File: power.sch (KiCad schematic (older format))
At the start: 0 parts

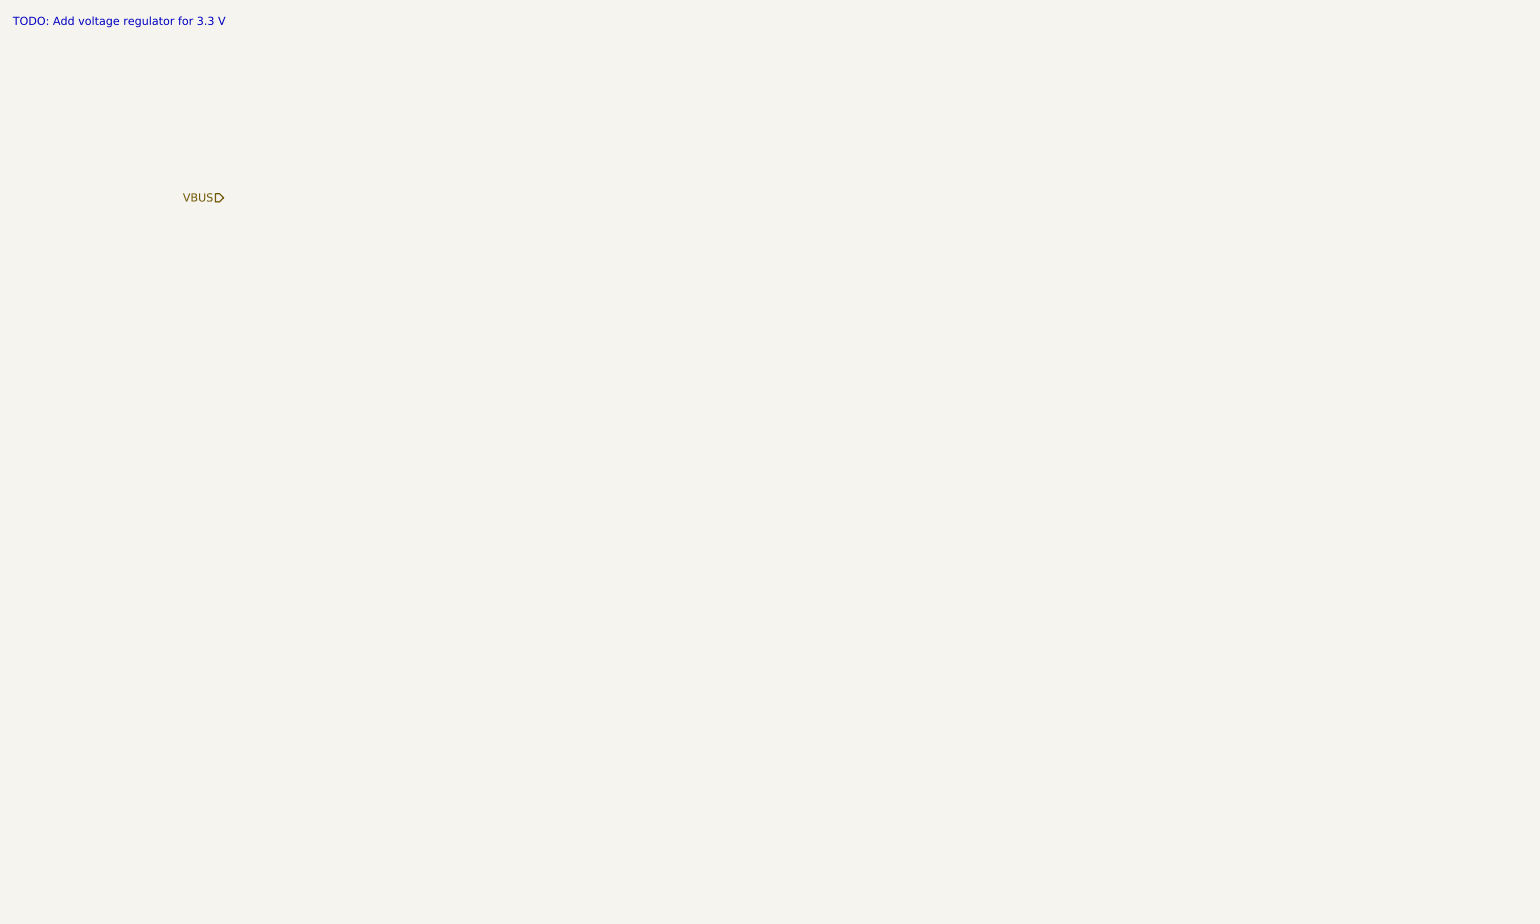
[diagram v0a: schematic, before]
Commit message: Complete muxing and level translation
Added Aux USB to avoid using a HUB, which don't seem to be too readily
available out there and would complicate the design for no good reason.

Now the i2c lines can also be switched.

Added voltage level translation up to 1.2V from 3.3V. Selected
bidirectional level translator.

Started looking into power supply.
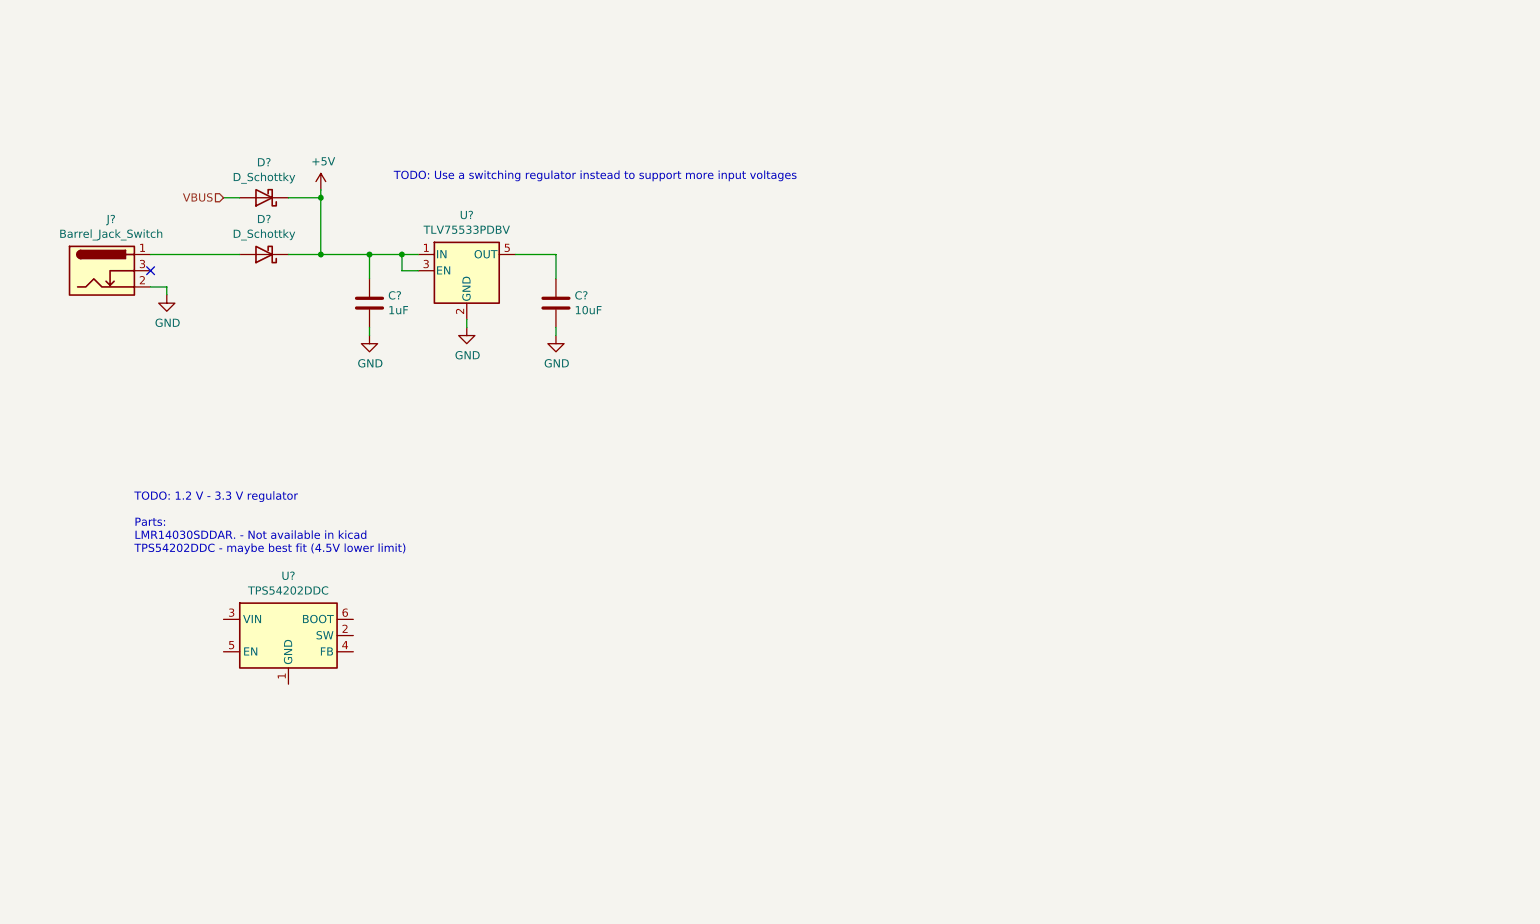
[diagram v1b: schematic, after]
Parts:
- added C?: 1uF, symbol Device:C
- added C?: 10uF, symbol Device:C
- added D? (x2): D_Schottky, symbol Device:D_Schottky
- added J?: Barrel_Jack_Switch, symbol Connector:Barrel_Jack_Switch
- added U?: TLV75533PDBV, Package_TO_SOT_SMD:SOT-23-5, symbol Regulator_Linear:TLV75533PDBV
- added U?: TPS54202DDC, Package_TO_SOT_SMD:SOT-23-6, symbol Regulator_Switching:TPS54202DDC
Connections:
- net VBUS: now also D?.2 (A)
- new net: D?.2 (A), J?.1
- new net: C?.1, U?.5 (OUT)
- new net +5V: C?.1, D?.1 (K), D?.1 (K), U?.1 (IN), U?.3 (EN)
- new net GND: C?.2, C?.2, J?.2, U?.2 (GND)
- no-connect marks 0 -> 1
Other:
- note added: "TODO: 1.2 V - 3.3 V regulator\n\nParts:\nLMR14030SDDAR. - Not available in kicad\nTPS54202DDC - maybe best fit (4.5V lower limit)"
- note added: "TODO: Use a switching regulator instead to support more input voltages"
- note removed: "TODO: Add voltage regulator for 3.3 V"
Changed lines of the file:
@@
 $Descr A4 11693 8268
 encoding utf-8
-Sheet 9 9
+Sheet 11 12
 Title ""
 Date ""
@@
 Text HLabel 2100 1850 0    50   Input ~ 0
 VBUS
-Text Notes 800  800  0    50   ~ 0
-TODO: Add voltage regulator for 3.3 V
+Text Notes 3150 1750 0    50   ~ 0
+TODO: Use a switching regulator instead to support more input voltages
+$Comp
+L Device:D_Schottky D?
+U 1 1 61C1AC34
+P 2350 1850
+F 0 "D?" H 2350 1633 50  0000 C CNN
+F 1 "D_Schottky" H 2350 1724 50  0000 C CNN
+F 2 "" H 2350 1850 50  0001 C CNN
+F 3 "~" H 2350 1850 50  0001 C CNN
+	1    2350 1850
+	-1   0    0    1
+$EndComp
+Wire Wire Line
+	2100 1850 2200 1850
+$Comp
+L power:+5V #PWR?
+U 1 1 61C1BC9B
+P 2700 1800
+F 0 "#PWR?" H 2700 1650 50  0001 C CNN
+F 1 "+5V" H 2715 1973 50  0000 C CNN
+F 2 "" H 2700 1800 50  0001 C CNN
+F 3 "" H 2700 1800 50  0001 C CNN
+	1    2700 1800
+	1    0    0    -1
+$EndComp
+Wire Wire Line
+	2700 1850 2500 1850
+Wire Wire Line
+	2700 1800 2700 1850
+$Comp
+L Device:D_Schottky D?
+U 1 1 61C24E59
+P 2350 2200
+F 0 "D?" H 2350 1983 50  0000 C CNN
+F 1 "D_Schottky" H 2350 2074 50  0000 C CNN
+F 2 "" H 2350 2200 50  0001 C CNN
+F 3 "~" H 2350 2200 50  0001 C CNN
+	1    2350 2200
+	-1   0    0    1
+$EndComp
+Wire Wire Line
+	2700 2200 2500 2200
+$Comp
+L Connector:Barrel_Jack_Switch J?
+U 1 1 61C25710
+P 1350 2300
+F 0 "J?" H 1407 2617 50  0000 C CNN
+F 1 "Barrel_Jack_Switch" H 1407 2526 50  0000 C CNN
+F 2 "" H 1400 2260 50  0001 C CNN
+F 3 "~" H 1400 2260 50  0001 C CNN
+	1    1350 2300
+	1    0    0    -1
+$EndComp
+NoConn ~ 1650 2300
+Wire Wire Line
+	1650 2200 2200 2200
+$Comp
+L power:GND #PWR?
+U 1 1 61C2675F
+P 1750 2450
+F 0 "#PWR?" H 1750 2200 50  0001 C CNN
+F 1 "GND" H 1755 2277 50  0000 C CNN
+F 2 "" H 1750 2450 50  0001 C CNN
+F 3 "" H 1750 2450 50  0001 C CNN
+	1    1750 2450
+	1    0    0    -1
+$EndComp
+Wire Wire Line
+	1650 2400 1750 2400
+Wire Wire Line
+	1750 2400 1750 2450
+Connection ~ 2700 1850
+$Comp
+L Regulator_Linear:TLV75533PDBV U?
+U 1 1 61C284A0
+P 3600 2300
+F 0 "U?" H 3600 2642 50  0000 C CNN
+F 1 "TLV75533PDBV" H 3600 2551 50  0000 C CNN
+F 2 "Package_TO_SOT_SMD:SOT-23-5" H 3600 2625 50  0001 C CIN
+F 3 "http://www.ti.com/lit/ds/symlink/tlv755p.pdf" H 3600 2350 50  0001 C CNN
+	1    3600 2300
+	1    0    0    -1
+$EndComp
+$Comp
+L power:GND #PWR?
+U 1 1 61C2CA61
+P 3600 2650
+F 0 "#PWR?" H 3600 2400 50  0001 C CNN
+F 1 "GND" H 3605 2477 50  0000 C CNN
+F 2 "" H 3600 2650 50  0001 C CNN
+F 3 "" H 3600 2650 50  0001 C CNN
+	1    3600 2650
+	1    0    0    -1
+$EndComp
+Wire Wire Line
+	3600 2600 3600 2650
+Wire Wire Line
+	2700 1850 2700 2200
+Wire Wire Line
+	3300 2200 3200 2200
+Connection ~ 2700 2200
+Wire Wire Line
+	3300 2300 3200 2300
+Wire Wire Line
+	3200 2300 3200 2200
+Connection ~ 3200 2200
+Wire Wire Line
+	3200 2200 3000 2200
+$Comp
+L Device:C C?
+U 1 1 61C304EB
+P 3000 2500
+F 0 "C?" H 3115 2546 50  0000 L CNN
+F 1 "1uF" H 3115 2455 50  0000 L CNN
+F 2 "" H 3038 2350 50  0001 C CNN
+F 3 "~" H 3000 2500 50  0001 C CNN
+	1    3000 2500
+	1    0    0    -1
+$EndComp
+$Comp
+L power:GND #PWR?
+U 1 1 61C30A39
+P 3000 2700
+F 0 "#PWR?" H 3000 2450 50  0001 C CNN
+F 1 "GND" H 3005 2527 50  0000 C CNN
+F 2 "" H 3000 2700 50  0001 C CNN
+F 3 "" H 3000 2700 50  0001 C CNN
+	1    3000 2700
+	1    0    0    -1
+$EndComp
+Wire Wire Line
+	3000 2350 3000 2200
+Connection ~ 3000 2200
+Wire Wire Line
+	3000 2200 2700 2200
+Wire Wire Line
+	3000 2700 3000 2650
+$Comp
+L Device:C C?
+U 1 1 61C31905
+P 4150 2500
+F 0 "C?" H 4265 2546 50  0000 L CNN
+F 1 "10uF" H 4265 2455 50  0000 L CNN
+F 2 "" H 4188 2350 50  0001 C CNN
+F 3 "~" H 4150 2500 50  0001 C CNN
+	1    4150 2500
+	1    0    0    -1
+$EndComp
+$Comp
+L power:GND #PWR?
+U 1 1 61C3190B
+P 4150 2700
+F 0 "#PWR?" H 4150 2450 50  0001 C CNN
+F 1 "GND" H 4155 2527 50  0000 C CNN
+F 2 "" H 4150 2700 50  0001 C CNN
+F 3 "" H 4150 2700 50  0001 C CNN
+	1    4150 2700
+	1    0    0    -1
+$EndComp
+Wire Wire Line
+	4150 2700 4150 2650
+Wire Wire Line
+	3900 2200 4150 2200
+Wire Wire Line
+	4150 2200 4150 2350
+Text Notes 1550 4050 0    50   ~ 0
+TODO: 1.2 V - 3.3 V regulator\n\nParts:\nLMR14030SDDAR. - Not available in kicad\nTPS54202DDC - maybe best fit (4.5V lower limit)
+$Comp
+L Regulator_Switching:TPS54202DDC U?
+U 1 1 61C416E7
+P 2500 4550
+F 0 "U?" H 2500 4917 50  0000 C CNN
+F 1 "TPS54202DDC" H 2500 4826 50  0000 C CNN
+F 2 "Package_TO_SOT_SMD:SOT-23-6" H 2550 4200 50  0001 L CNN
+F 3 "http://www.ti.com/lit/ds/symlink/tps54202.pdf" H 2200 4900 50  0001 C CNN
+	1    2500 4550
+	1    0    0    -1
+$EndComp
 $EndSCHEMATC

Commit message: Add initial power design
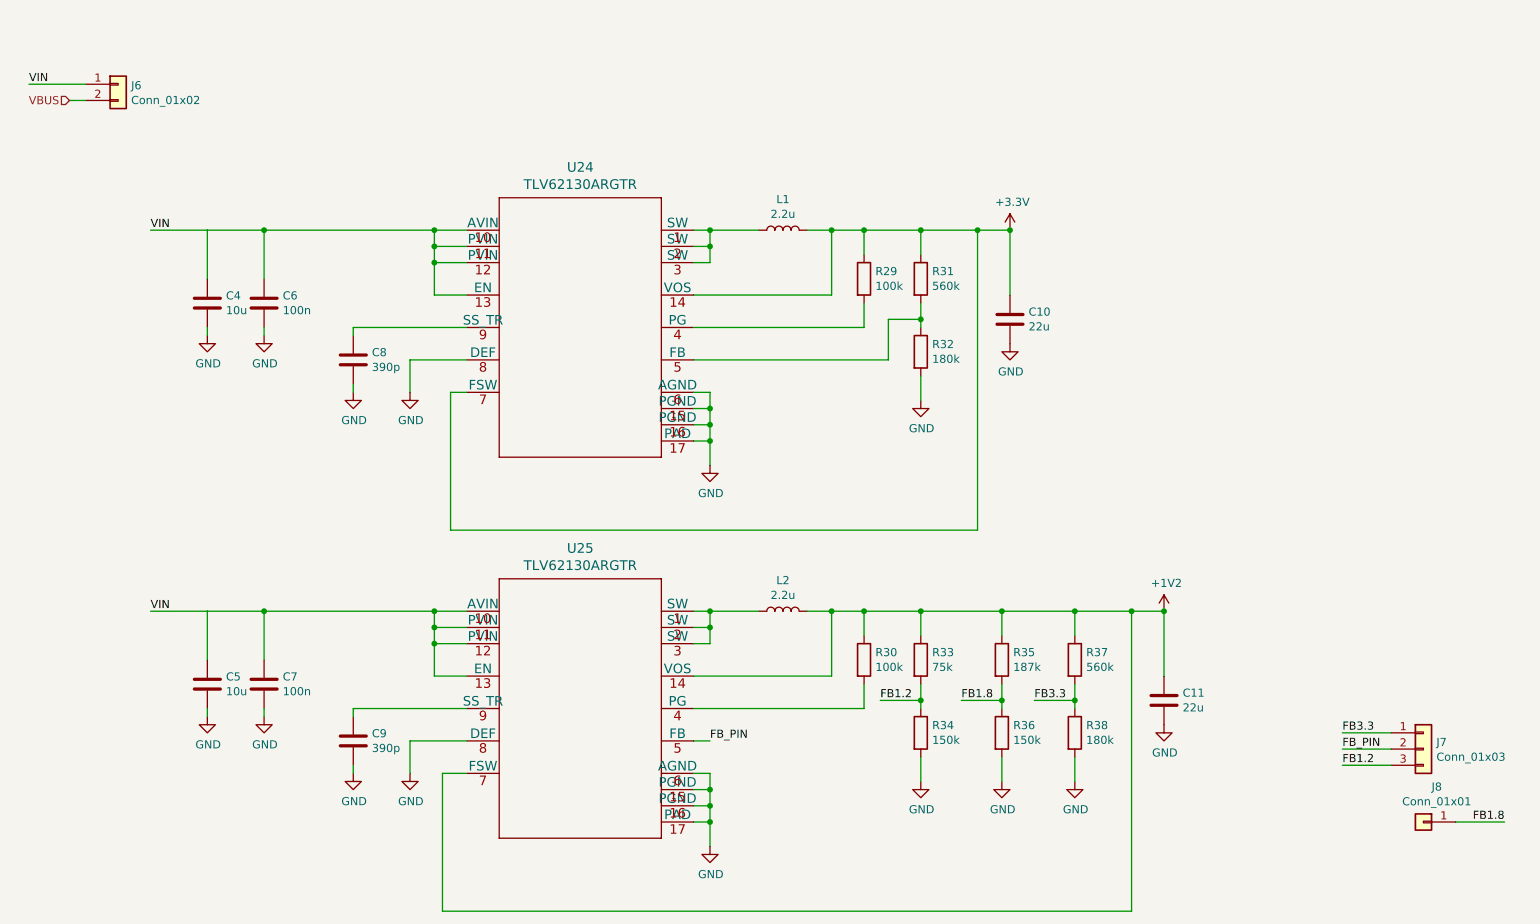
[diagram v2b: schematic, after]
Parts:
- removed C?: 1uF, symbol Device:C
- removed C?: 10uF, symbol Device:C
- removed D? (x2): D_Schottky, symbol Device:D_Schottky
- removed J?: Barrel_Jack_Switch, symbol Connector:Barrel_Jack_Switch
- removed U?: TLV75533PDBV, Package_TO_SOT_SMD:SOT-23-5, symbol Regulator_Linear:TLV75533PDBV
- removed U?: TPS54202DDC, Package_TO_SOT_SMD:SOT-23-6, symbol Regulator_Switching:TPS54202DDC
- added C10, C11: 22u, symbol Device:C
- added C4, C5: 10u, symbol Device:C
- added C6, C7: 100n, symbol Device:C
- added C8, C9: 390p, symbol Device:C
- added J6: Conn_01x02, symbol Connector_Generic:Conn_01x02
- added J7: Conn_01x03, symbol Connector_Generic:Conn_01x03
- added J8: Conn_01x01, symbol Connector_Generic:Conn_01x01
- added L1, L2: 2.2u, symbol Device:L
- added R29, R30: 100k, symbol Device:R
- added R31, R37: 560k, symbol Device:R
- added R32, R38: 180k, symbol Device:R
- added R33: 75k, symbol Device:R
- added R34, R36: 150k, symbol Device:R
- added R35: 187k, symbol Device:R
- added U24, U25: TLV62130ARGTR, RGT0016C, symbol TIRegulators:TLV62130ARGTR
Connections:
- net GND: now also C10.2, C11.2, C4.2, C5.2, C6.2, C7.2, C8.2, C9.2, R32.2, R34.2, R36.2, R38.2, U24.15 (PGND), U24.16 (PGND), U24.17 (PAD), U24.6 (AGND), U24.8 (DEF), U25.15 (PGND), U25.16 (PGND), U25.17 (PAD), U25.6 (AGND), U25.8 (DEF)
- net VBUS: now also J6.2 (Pin_2)
- new net: L1.1, U24.1 (SW), U24.2 (SW), U24.3 (SW)
- new net: R29.2, U24.4 (PG)
- new net: R31.2, R32.1, U24.5 (FB)
- new net: C8.1, U24.9 (SS_TR)
- new net: L2.1, U25.1 (SW), U25.2 (SW), U25.3 (SW)
- new net: R30.2, U25.4 (PG)
- new net: C9.1, U25.9 (SS_TR)
- new net +1V2: C11.1, L2.2, R30.1, R33.1, R35.1, R37.1, U25.14 (VOS), U25.7 (FSW)
- new net +3V3: C10.1, L1.2, R29.1, R31.1, U24.14 (VOS), U24.7 (FSW)
- new net FB1.2: J7.3 (Pin_3), R33.2, R34.1
- new net FB1.8: J8.1 (Pin_1), R35.2, R36.1
- new net FB3.3: J7.1 (Pin_1), R37.2, R38.1
- new net FB_PIN: J7.2 (Pin_2), U25.5 (FB)
- new net VIN: C4.1, C5.1, C6.1, C7.1, J6.1 (Pin_1), U24.10 (AVIN), U24.11 (PVIN), U24.12 (PVIN), U24.13 (EN), U25.10 (AVIN), U25.11 (PVIN), U25.12 (PVIN), U25.13 (EN)
- no-connect marks 1 -> 0
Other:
- note removed: "TODO: 1.2 V - 3.3 V regulator\n\nParts:\nLMR14030SDDAR. - Not available in kicad\nTPS54202DDC - maybe best fit (4.5V lower limit)"
- note removed: "TODO: Use a switching regulator instead to support more input voltages"

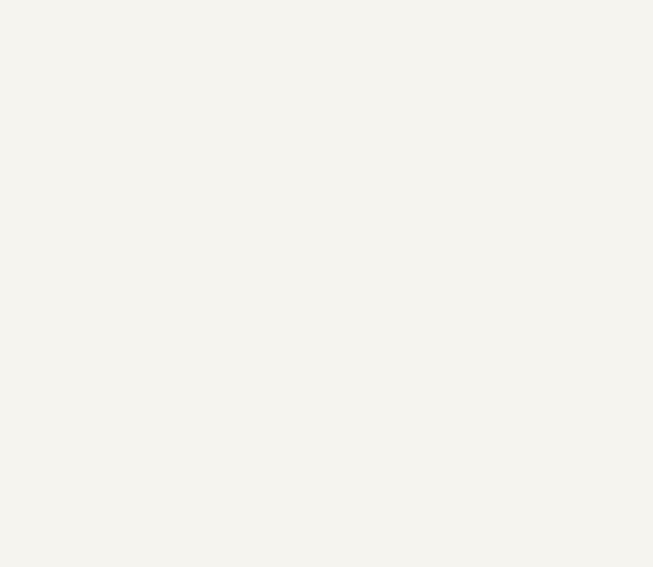
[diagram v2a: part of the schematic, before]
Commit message: Supply caps, initial signal states and headers
  * Added bulk supply caps.
  * Set initial control signal states via resistors.
  * Add debug headers.
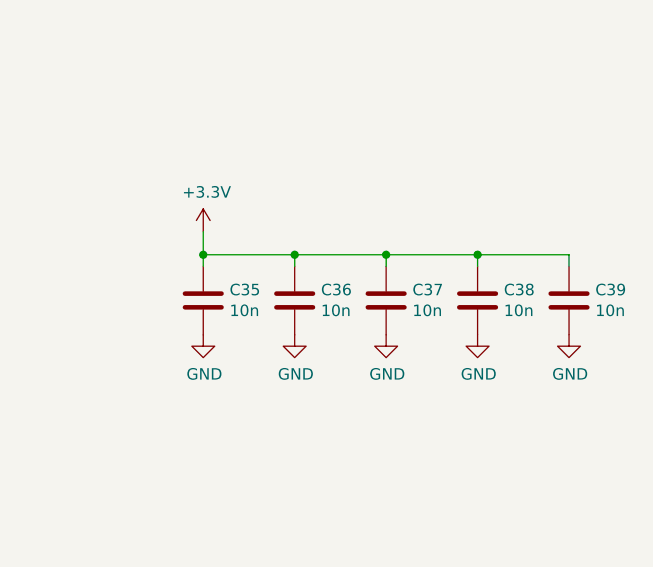
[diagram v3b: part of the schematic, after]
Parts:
- added C35, C36, C37, C38, C39: 10n, symbol Device:C
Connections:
- net +3V3: now also C35.1, C36.1, C37.1, C38.1, C39.1
- net GND: now also C35.2, C36.2, C37.2, C38.2, C39.2
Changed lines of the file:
@@
 Wire Wire Line
 	7700 4400 7350 4400
+$Comp
+L Device:C C35
+U 1 1 61AFDC5F
+P 8250 2400
+F 0 "C35" H 8365 2446 50  0000 L CNN
+F 1 "10n" H 8365 2355 50  0000 L CNN
+F 2 "" H 8288 2250 50  0001 C CNN
+F 3 "~" H 8250 2400 50  0001 C CNN
+	1    8250 2400
+	1    0    0    -1
+$EndComp
+$Comp
+L power:GND #PWR0185
+U 1 1 61AFDC66
+P 8250 2550
+F 0 "#PWR0185" H 8250 2300 50  0001 C CNN
+F 1 "GND" H 8255 2377 50  0000 C CNN
+F 2 "" H 8250 2550 50  0001 C CNN
+F 3 "" H 8250 2550 50  0001 C CNN
+	1    8250 2550
+	1    0    0    -1
+$EndComp
+$Comp
+L power:+3.3V #PWR0186
+U 1 1 61B028B4
+P 8250 2100
+F 0 "#PWR0186" H 8250 1950 50  0001 C CNN
+F 1 "+3.3V" H 8265 2273 50  0000 C CNN
+F 2 "" H 8250 2100 50  0001 C CNN
+F 3 "" H 8250 2100 50  0001 C CNN
+	1    8250 2100
+	1    0    0    -1
+$EndComp
+$Comp
+L Device:C C36
+U 1 1 61B0E783
+P 8650 2400
+F 0 "C36" H 8765 2446 50  0000 L CNN
+F 1 "10n" H 8765 2355 50  0000 L CNN
+F 2 "" H 8688 2250 50  0001 C CNN
+F 3 "~" H 8650 2400 50  0001 C CNN
+	1    8650 2400
+	1    0    0    -1
+$EndComp
+$Comp
+L power:GND #PWR0187
+U 1 1 61B0E789
+P 8650 2550
+F 0 "#PWR0187" H 8650 2300 50  0001 C CNN
+F 1 "GND" H 8655 2377 50  0000 C CNN
+F 2 "" H 8650 2550 50  0001 C CNN
+F 3 "" H 8650 2550 50  0001 C CNN
+	1    8650 2550
+	1    0    0    -1
+$EndComp
+$Comp
+L Device:C C37
+U 1 1 61B127B9
+P 9050 2400
+F 0 "C37" H 9165 2446 50  0000 L CNN
+F 1 "10n" H 9165 2355 50  0000 L CNN
+F 2 "" H 9088 2250 50  0001 C CNN
+F 3 "~" H 9050 2400 50  0001 C CNN
+	1    9050 2400
+	1    0    0    -1
+$EndComp
+$Comp
+L power:GND #PWR0188
+U 1 1 61B127BF
+P 9050 2550
+F 0 "#PWR0188" H 9050 2300 50  0001 C CNN
+F 1 "GND" H 9055 2377 50  0000 C CNN
+F 2 "" H 9050 2550 50  0001 C CNN
+F 3 "" H 9050 2550 50  0001 C CNN
+	1    9050 2550
+	1    0    0    -1
+$EndComp
+$Comp
+L Device:C C38
+U 1 1 61B168F9
+P 9450 2400
+F 0 "C38" H 9565 2446 50  0000 L CNN
+F 1 "10n" H 9565 2355 50  0000 L CNN
+F 2 "" H 9488 2250 50  0001 C CNN
+F 3 "~" H 9450 2400 50  0001 C CNN
+	1    9450 2400
+	1    0    0    -1
+$EndComp
+$Comp
+L power:GND #PWR0189
+U 1 1 61B168FF
+P 9450 2550
+F 0 "#PWR0189" H 9450 2300 50  0001 C CNN
+F 1 "GND" H 9455 2377 50  0000 C CNN
+F 2 "" H 9450 2550 50  0001 C CNN
+F 3 "" H 9450 2550 50  0001 C CNN
+	1    9450 2550
+	1    0    0    -1
+$EndComp
+$Comp
+L Device:C C39
+U 1 1 61B1AB81
+P 9850 2400
+F 0 "C39" H 9965 2446 50  0000 L CNN
+F 1 "10n" H 9965 2355 50  0000 L CNN
+F 2 "" H 9888 2250 50  0001 C CNN
+F 3 "~" H 9850 2400 50  0001 C CNN
+	1    9850 2400
+	1    0    0    -1
+$EndComp
+$Comp
+L power:GND #PWR0190
+U 1 1 61B1AB87
+P 9850 2550
+F 0 "#PWR0190" H 9850 2300 50  0001 C CNN
+F 1 "GND" H 9855 2377 50  0000 C CNN
+F 2 "" H 9850 2550 50  0001 C CNN
+F 3 "" H 9850 2550 50  0001 C CNN
+	1    9850 2550
+	1    0    0    -1
+$EndComp
+Wire Wire Line
+	9850 2250 9850 2200
+Wire Wire Line
+	9850 2200 9450 2200
+Wire Wire Line
+	8250 2200 8250 2100
+Wire Wire Line
+	8250 2200 8250 2250
+Connection ~ 8250 2200
+Wire Wire Line
+	8650 2200 8650 2250
+Connection ~ 8650 2200
+Wire Wire Line
+	8650 2200 8250 2200
+Wire Wire Line
+	9050 2200 9050 2250
+Connection ~ 9050 2200
+Wire Wire Line
+	9050 2200 8650 2200
+Wire Wire Line
+	9450 2200 9450 2250
+Connection ~ 9450 2200
+Wire Wire Line
+	9450 2200 9050 2200
 $EndSCHEMATC

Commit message: Replace MCU by something available in distributors
Given the current chip shortage the STM32F0 was not available from
JLCPCB. This one (STM32F411CE) is available in large quantities from
JLCPCB. Despite being much more powerful than the F0, it is still in the
price range and actually cheaper than the STM32F103C8T6... which I don't
understand...
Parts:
- U24, U25: LCSC (none) -> C138520
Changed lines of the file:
@@
 $Descr A4 11693 8268
 encoding utf-8
-Sheet 11 12
+Sheet 10 12
 Title ""
 Date ""
@@
 F 2 "RGT0016C" H 4300 2590 60  0001 C CNN
 F 3 "" H 4300 2650 60  0000 C CNN
+F 4 "C138520" H 4300 2650 50  0001 C CNN "LCSC"
 	1    4300 2650
 	1    0    0    -1
@@
 F 2 "RGT0016C" H 4300 4940 60  0001 C CNN
 F 3 "" H 4300 5000 60  0000 C CNN
+F 4 "C138520" H 4300 5000 50  0001 C CNN "LCSC"
 	1    4300 5000
 	1    0    0    -1
